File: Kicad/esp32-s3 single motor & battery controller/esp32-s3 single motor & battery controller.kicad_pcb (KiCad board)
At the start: 4 copper layers, 30.4 x 40.3 mm, 132 parts, among them J1 JST SH SM04B, J2 7 pin FPC 0.3mm, J3 Conn_01x03, J4 Conn_01x03, J5 Batt Balance connector, Q1 NMOS,12v, Q2 NMOS, 12v, Q3 NMOS,12v,PPak, Q4 NMOS, 12v, Q5 NMOS, 12v, Q7 NMOS,12v,PPak, SW1 SW_Push, SW2 SW_Push, U2 AP63203WU, U3 BQ76905RGRR, U4 BQ24780SRUYR, U5 ESP32-S3, U6 74HC595, Y1 40mhz, 10ppm

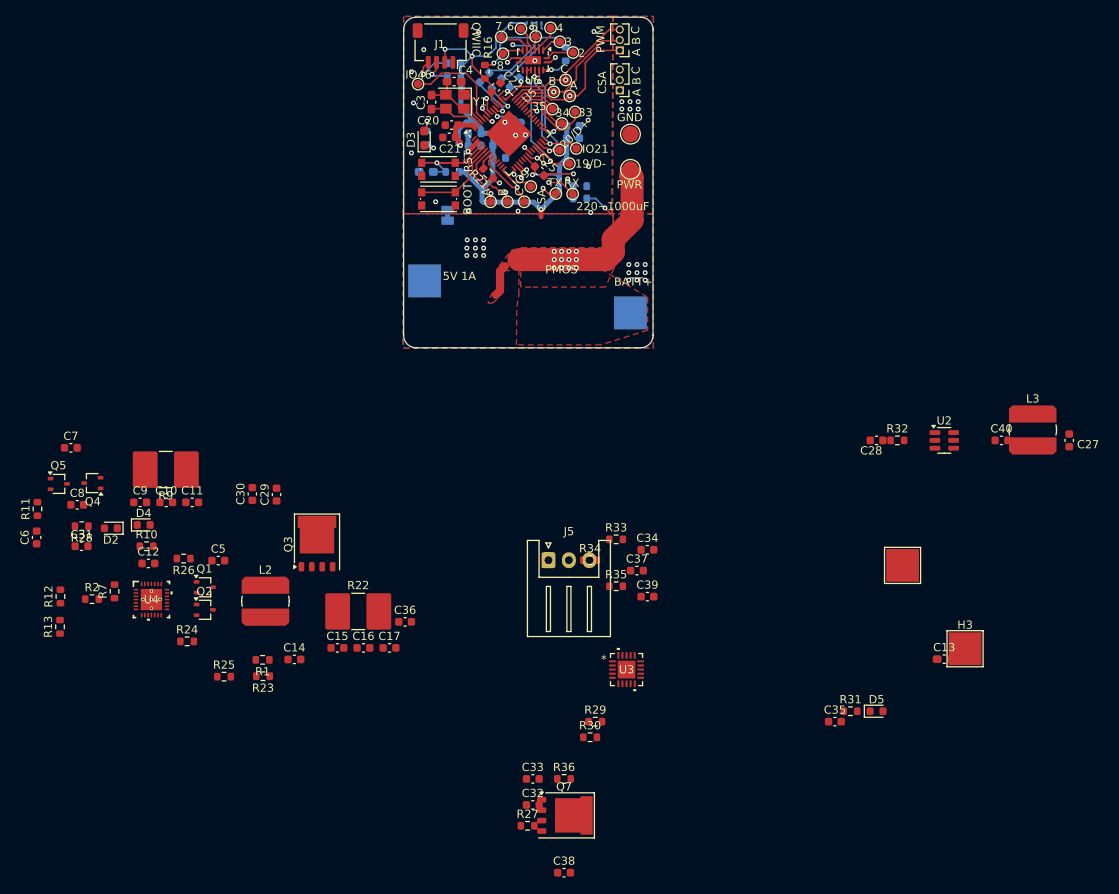
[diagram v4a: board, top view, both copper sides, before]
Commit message: Basic component layout complete
This will still change as I start wiring and switch out parts, but the basic layout is complete. 20x65mm, but my goal is 15x45mm for the size.
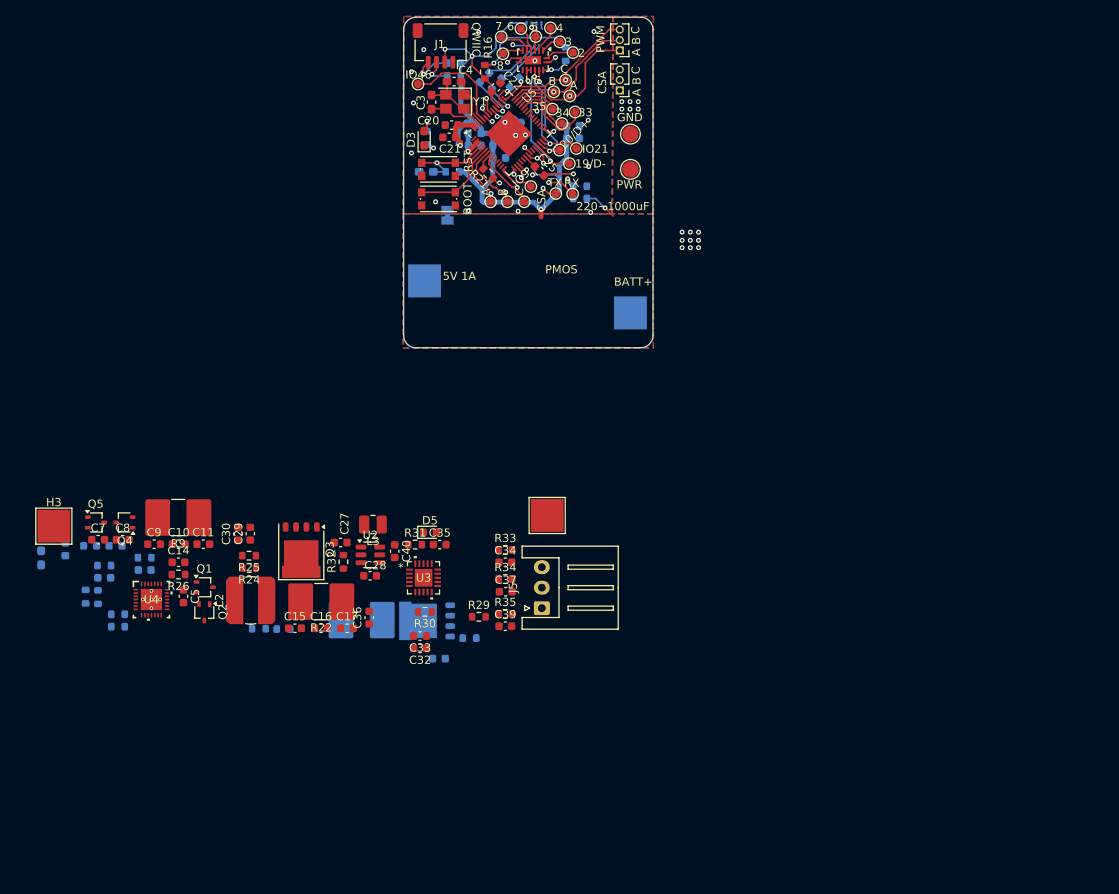
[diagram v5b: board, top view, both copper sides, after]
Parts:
- C12, C13, C31, C38, C6, D2, D4, Q7, R1, R10, R11, R12, R13, R2, R23, R28, R36, R7: moved to B.Cu
- L3: footprint Inductor_SMD:L_Bourns_SDR0604 -> Inductor_SMD:L_1008_2520Metric
- R27: value 10mOhm -> 10mOhm, CS; footprint Resistor_SMD:R_0603_1608Metric -> Resistor_SMD:R_2816_7142Metric; moved to B.Cu
- moved H3 112.1 mm to (80.0, 152.0)
- moved C13 110.8 mm to (78.5, 155.9), turned to 90 degrees
- moved C27 89.7 mm to (115.0, 154.0), turned to 180 degrees
- moved L3 81.3 mm to (118.9, 151.8), turned to 180 degrees
- moved C40 75.2 mm to (121.6, 155.1), turned to -90 degrees
- moved U2 71.4 mm to (118.6, 155.5)
- moved R32 69.1 mm to (115.3, 156.3), turned to 90 degrees
- moved C28 63.9 mm to (118.6, 158.1), turned to 0 degrees
- moved D5 58.7 mm to (125.8, 152.8)
- moved R31 56.8 mm to (124.0, 154.2)
- moved C35 52.8 mm to (127.0, 154.2)
- moved H1 43.8 mm to (140.2, 150.7)
- moved R27 32.2 mm to (117.5, 163.5), turned to 180 degrees
- moved C38 30.2 mm to (127.0, 168.2)
- moved Q7 29.0 mm to (125.6, 163.6), turned to 180 degrees
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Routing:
- net /MOTORPWR: track 33.5 -> 4.12 mm, vias 13 -> 1
- net GNDPWR: vias 24 -> 15
- removed copper zone on F.Cu, net /MOTORPWR
- removed copper zone on F.Cu, net /PSU/BATT+

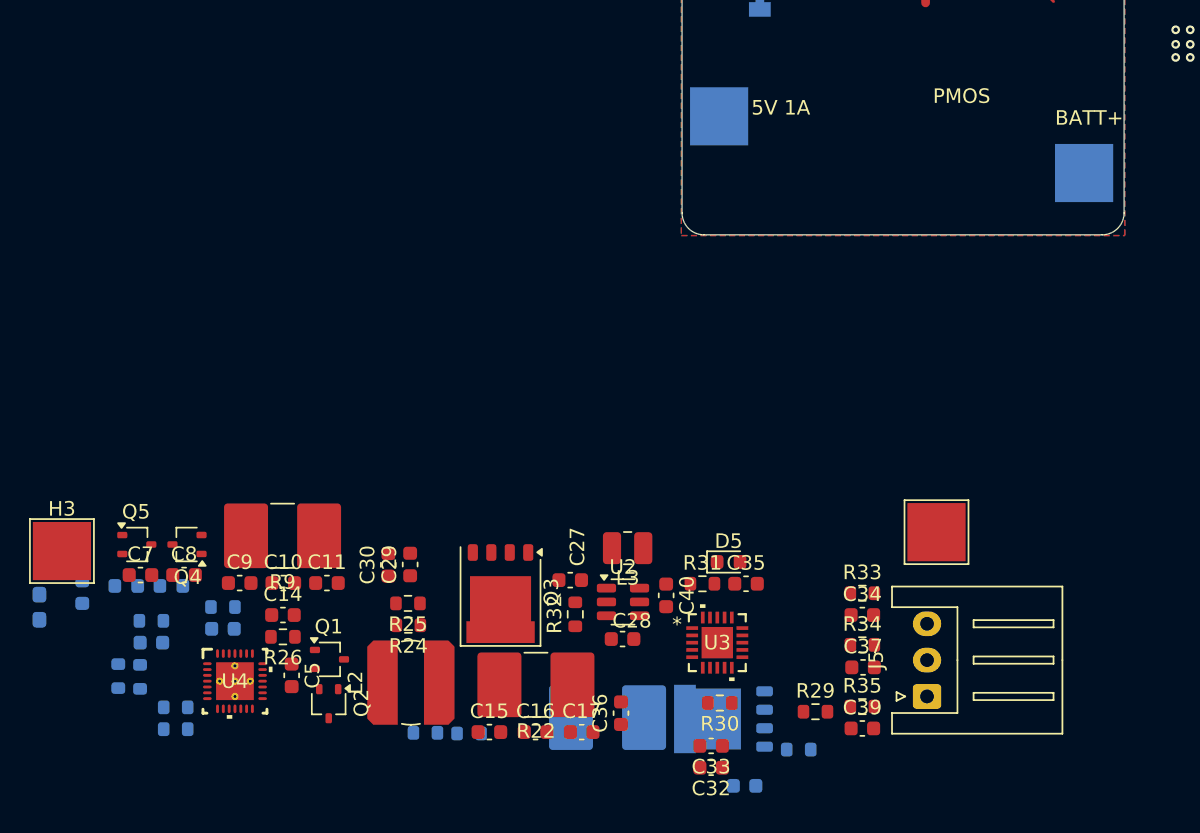
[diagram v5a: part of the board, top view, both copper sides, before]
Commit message: Reached target dimensions of 15x45mm
I imagine heat will be crazy, but hey, its small!
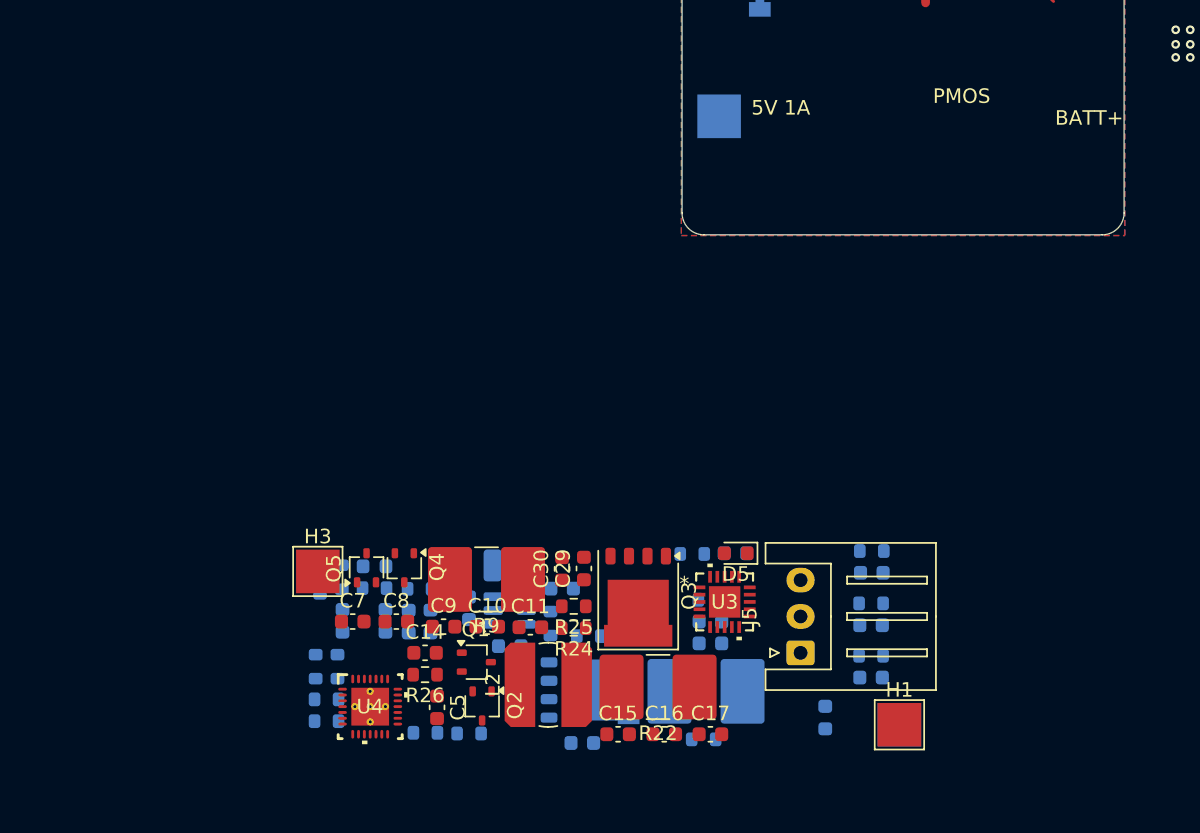
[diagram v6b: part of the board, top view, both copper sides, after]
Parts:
- C27, C28, C32, C33, C34, C35, C36, C37, C39, C40, L3, R29, R30, R31, R32, R33, R34, R35, U2: moved to B.Cu
- H1, H2, H3, H4: value 4mm_Pad -> Pad; footprint TestPoint:TestPoint_Pad_4.0x4.0mm -> TestPoint:TestPoint_Pad_3.0x3.0mm
- moved H2 40.0 mm to (137.6, 163.9)
- moved D4 21.1 mm to (105.3, 156.8), turned to -90 degrees
- moved C13 19.4 mm to (97.8, 153.9), turned to -90 degrees
- moved R10 18.6 mm to (104.6, 154.6), turned to 0 degrees
- moved C6 18.0 mm to (99.3, 156.8), turned to -90 degrees
- moved R11 17.9 mm to (99.2, 153.8)
- moved C12 17.8 mm to (103.8, 156.8), turned to -90 degrees
- moved H3 17.7 mm to (97.6, 153.4)
- moved R36 16.4 mm to (116.2, 157.8)
- moved Q5 15.9 mm to (101.0, 153.2), turned to 90 degrees
- moved R7 15.1 mm to (99.0, 159.9)
- moved Q4 15.0 mm to (103.5, 153.2), turned to -90 degrees
- moved C7 14.9 mm to (100.0, 156.8)
- moved C8 14.9 mm to (103.0, 156.8)
- moved C10 14.3 mm to (109.2, 157.2)
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
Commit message: Started wiring
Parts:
- R36: moved to F.Cu
- moved C36 42.1 mm to (150.4, 125.4)
- moved R32 39.3 mm to (133.3, 122.9)
- moved L3 39.3 mm to (130.4, 118.9)
- moved U2 39.3 mm to (130.5, 122.0)
- moved C27 39.3 mm to (134.1, 120.5)
- moved C40 39.3 mm to (127.7, 121.9)
- moved R36 39.2 mm to (139.1, 126.0), turned to 0 degrees
- moved R23 38.6 mm to (123.5, 130.6), turned to 180 degrees
- moved C28 38.5 mm to (128.9, 124.5)
- moved C31 37.3 mm to (117.5, 122.8)
- moved C6 37.3 mm to (114.6, 122.8)
- moved D2 37.3 mm to (116.8, 119.0)
- moved R11 37.3 mm to (114.5, 119.8)
- moved R28 37.3 mm to (116.8, 120.5)
- moved C12 37.3 mm to (119.2, 122.8)
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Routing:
- net /PSU/BATT+: track 0.00 -> 41.9 mm
- net /PSU/BATT-: track 0.00 -> 31.7 mm
- net Net-(Q1-S): track 0.00 -> 18.8 mm, vias 0 -> 2
- net Net-(Q7-S): track 0.00 -> 18.5 mm
- net Net-(Q1-G): track 0.00 -> 11.0 mm, vias 0 -> 2
- net Net-(U4-BTST): track 0.00 -> 9.42 mm, vias 0 -> 2
- net /MOTORPWR: track 4.12 -> 13.5 mm
- net Net-(Q4-D): track 0.00 -> 8.07 mm
- net Net-(U2-SW): track 0.00 -> 7.69 mm
- net /PSU/IN: track 0.00 -> 7.50 mm
- net Net-(Q2-G): track 0.00 -> 7.40 mm
- net GNDPWR: track 1.27 -> 8.32 mm, vias 15 -> 16
- net Net-(Q4-G): track 0.00 -> 7.03 mm
- net Net-(D2-K): track 0.00 -> 5.27 mm
- net /PSU/REGN: track 0.00 -> 5.26 mm
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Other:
- board size 30.4 x 40.3 mm -> 44.9 x 42 mm

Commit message: Re-arranging some components, continue routing
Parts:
- R1, R12, R13, R23: moved to F.Cu
- moved R13 6.49 mm to (109.2, 123.3), turned to -90 degrees
- moved R12 5.01 mm to (110.7, 123.3), turned to 90 degrees
- moved R7 3.76 mm to (109.1, 129.4), turned to -90 degrees
- moved R1 3.56 mm to (117.0, 130.9)
- moved R23 3.51 mm to (120.0, 130.8)
- moved C5 3.30 mm to (117.2, 125.8), turned to 0 degrees
- moved C38 2.76 mm to (131.2, 131.2)
- moved C14 2.70 mm to (116.8, 127.8)
- moved R26 2.70 mm to (116.8, 129.3)
- moved U4 1.88 mm to (112.0, 127.4), turned to -90 degrees
- moved R2 0.80 mm to (109.2, 125.2)
- moved Q2 0.40 mm to (120.9, 128.4)
- moved Q1 0.39 mm to (120.5, 125.4)
- moved C7 0.33 mm to (112.9, 122.9)
- moved C8 0.33 mm to (115.9, 122.9)
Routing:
- net Net-(Q3-S): track 5.10 -> 36.6 mm
- net Net-(U4-BATDRV): track 0.00 -> 24.6 mm, vias 0 -> 2
- net Net-(U4-BATSRC): track 0.00 -> 22.2 mm, vias 0 -> 2
- net /PSU/BATT+: track 41.9 -> 59.9 mm
- net Net-(U4-SRN): track 0.00 -> 8.66 mm
- net Net-(Q4-S): track 0.00 -> 6.36 mm
- net Net-(U4-BTST): track 9.42 -> 3.48 mm, vias 2 -> 0
- net Net-(U4-ILIM): track 0.00 -> 5.14 mm
- net /PSU/IN: track 7.50 -> 12.1 mm
- net GNDPWR: track 8.32 -> 12.9 mm, vias 16 -> 17
- net Net-(Q4-G): track 7.03 -> 11.6 mm, vias 0 -> 2
- net Net-(U4-SRP): track 0.00 -> 4.37 mm
- net Net-(Q3-G): track 0.00 -> 4.16 mm
- net Net-(Q1-G): track 11.0 -> 7.77 mm
- net Net-(Q1-S): track 18.8 -> 15.8 mm, vias 2 -> 0
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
